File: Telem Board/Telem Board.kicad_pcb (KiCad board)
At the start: 2 copper layers, 27 parts, among them J1 MAIN, J2 NTC1, J3 NTC2, J4 NTC3, J5 NTC4, J6 6S, U1 LM1117-3.3, U2 MCP3208

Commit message: route
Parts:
- removed C9: 1uF, Capacitor_SMD:C_0805_2012Metric_Pad1.18x1.45mm_HandSolder
- removed H3, H4: MountingHole, MountingHole:MountingHole_3.2mm_M3
- H1, H2: footprint MountingHole:MountingHole_3.2mm_M3 -> MountingHole:MountingHole_2.7mm_M2.5
- moved J4 65.3 mm to (144.1, 99.7), turned to 270 degrees
- moved R5 62.9 mm to (149.2, 80.4), turned to 270 degrees
- moved J3 60.9 mm to (144.1, 94.0), turned to 270 degrees
- moved J5 57.4 mm to (144.1, 105.4), turned to 270 degrees
- moved C5 57.0 mm to (156.8, 80.9), turned to 90 degrees
- moved R6 56.8 mm to (153.0, 80.4), turned to 90 degrees
- moved J2 56.0 mm to (144.1, 88.3), turned to 270 degrees
- moved C2 55.1 mm to (153.7, 92.9), turned to 90 degrees
- moved C4 53.1 mm to (153.7, 104.4), turned to 90 degrees
- moved H1 52.1 mm to (141.6, 76.8)
- moved C3 50.1 mm to (153.7, 98.7), turned to 90 degrees
- moved C7 48.1 mm to (177.2, 73.7), turned to 270 degrees
- moved C6 47.3 mm to (168.3, 80.6)
- moved R3 47.1 mm to (149.9, 98.1), turned to 270 degrees
- moved J1 47.0 mm to (179.1, 85.7)
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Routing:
- net +3V3: track 0.00 -> 68.5 mm, vias 0 -> 6
- net /CH5: track 0.00 -> 19.0 mm
- net +5V: track 0.00 -> 18.2 mm
- net /CH4: track 0.00 -> 16.6 mm
- net /CH2: track 0.00 -> 16.6 mm
- net /CH3: track 0.00 -> 15.2 mm
- net /SPI_SCK: track 0.00 -> 14.4 mm
- net /SPI_MOSI: track 0.00 -> 14.4 mm
- net /SPI_MISO: track 0.00 -> 14.4 mm
- net /ADC_CS: track 0.00 -> 14.4 mm
- net /CH0: track 0.00 -> 13.5 mm
- net Net-(J6-Pad1): track 0.00 -> 8.57 mm
- net GNDA: track 0.00 -> 3.91 mm, vias 0 -> 4
- added copper zone on B.Cu, net GNDA
- added copper zone on F.Cu, net GNDA
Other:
- board outline added: 43.2 x 43.8 mm
- board text added: "100K NTC thermistors"
- board text added: "5V"
- board text added: "6S LIPO IN"
- board text added: "CS"
- board text added: "GND"
- board text added: "MISO"
- board text added: "MOSI"
- board text added: "SCK"
- board text added: "TJUAV Telemetry board v0.1 Alan Hsu"

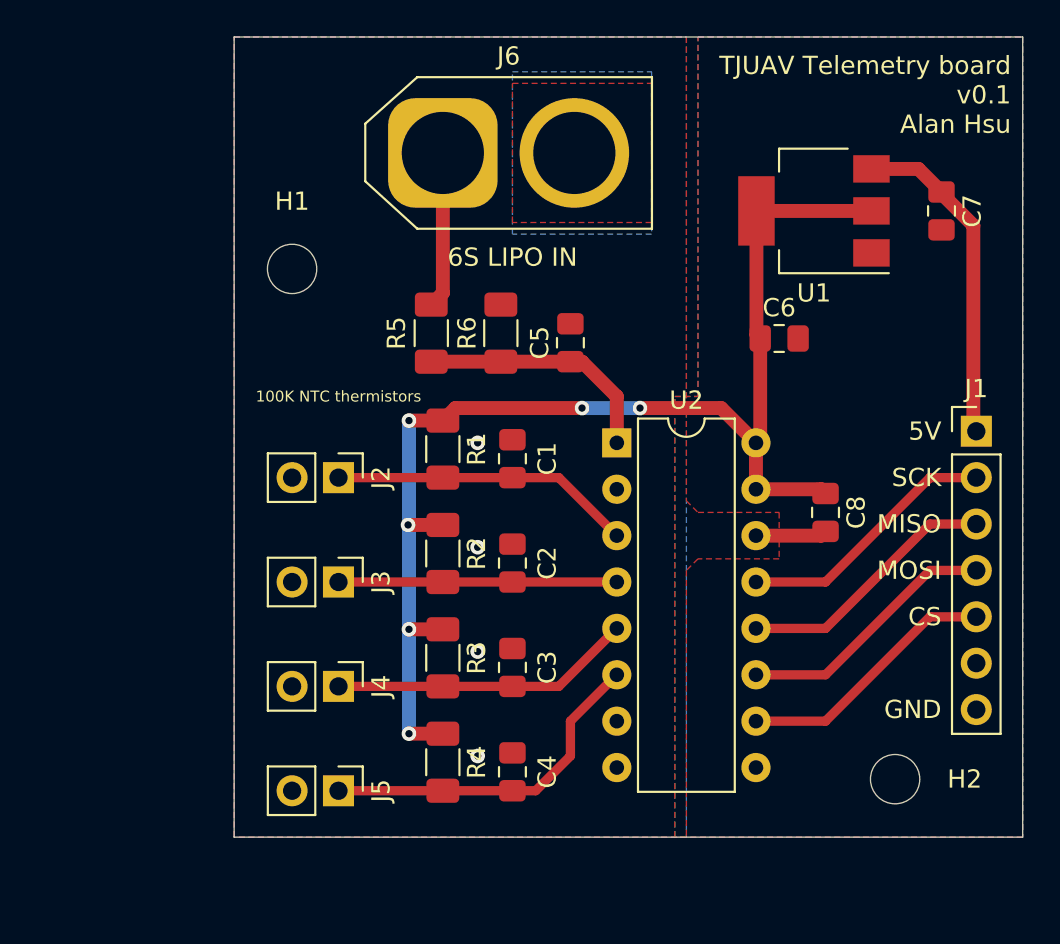
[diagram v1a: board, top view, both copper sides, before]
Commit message: add 3s battery in
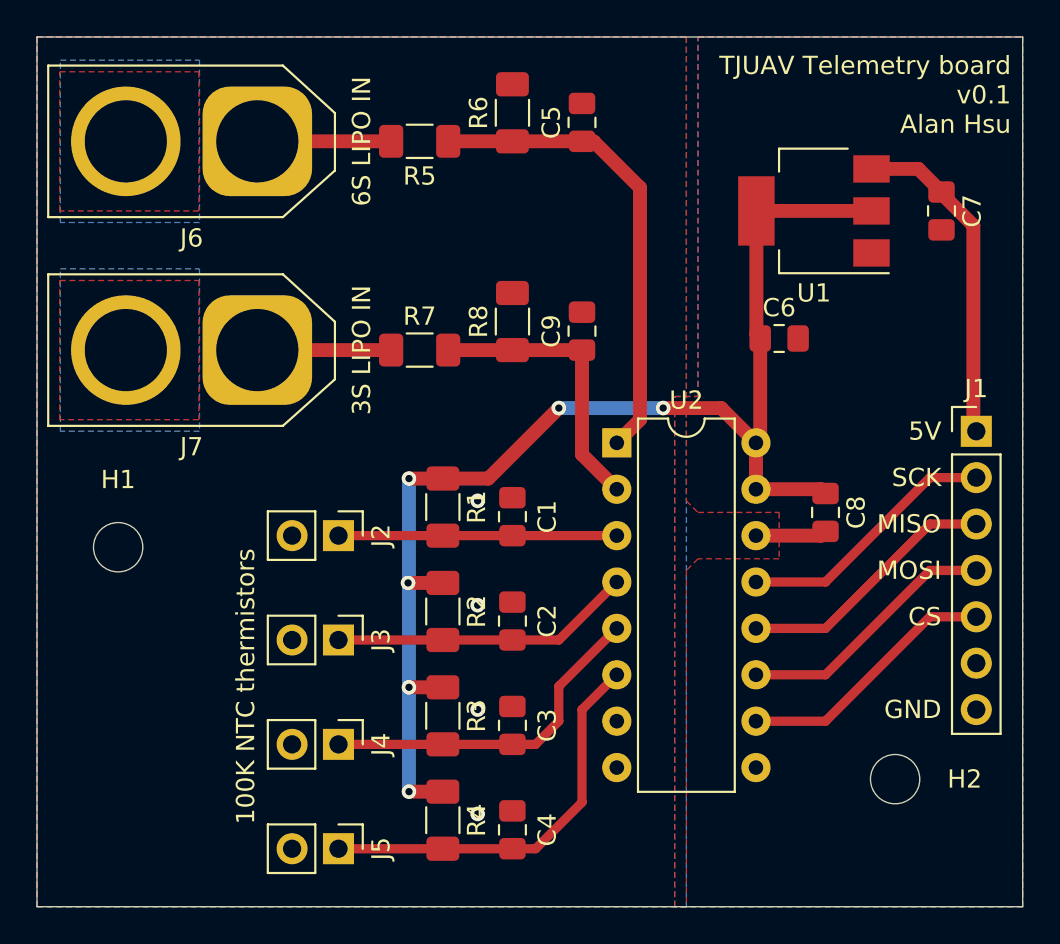
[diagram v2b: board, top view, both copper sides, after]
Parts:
- added C9: 0.47uF, Capacitor_SMD:C_0805_2012Metric_Pad1.18x1.45mm_HandSolder, F.Cu at (157.5, 80.2)
- added J7: 3S, Connector_AMASS:AMASS_XT60-M_1x02_P7.20mm_Vertical, F.Cu at (139.7, 81.3)
- added R7: 200K, Capacitor_SMD:C_1206_3216Metric_Pad1.33x1.80mm_HandSolder, F.Cu at (148.6, 81.3)
- added R8: 42K, Capacitor_SMD:C_1206_3216Metric_Pad1.33x1.80mm_HandSolder, F.Cu at (153.7, 79.7)
- moved H1 18.0 mm to (132.1, 92.1)
- moved R6 12.1 mm to (153.7, 68.3)
- moved C5 12.1 mm to (157.5, 68.8)
- moved R5 10.5 mm to (148.6, 69.8), turned to 0 degrees
- moved J6 10.2 mm to (139.7, 69.8), turned to 180 degrees
- moved C2 3.18 mm to (153.7, 96.1)
- moved J4 3.18 mm to (144.1, 102.9)
- moved R3 3.18 mm to (149.9, 101.3)
- moved C1 3.17 mm to (153.7, 90.4)
- moved C3 3.17 mm to (153.7, 101.8)
- moved C4 3.17 mm to (153.7, 107.5)
- moved J2 3.17 mm to (144.1, 91.4)
- moved J3 3.17 mm to (144.1, 97.2)
- moved J5 3.17 mm to (144.1, 108.6)
- moved R1 3.17 mm to (149.9, 89.9)
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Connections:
- U2 pad 2: (no net) -> /CH1
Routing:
- net /CH1: track 0.00 -> 15.7 mm
- net /CH0: track 13.5 -> 26.1 mm
- net Net-(J7-Pad1): track 0.00 -> 7.33 mm
- net /CH5: track 19.0 -> 22.2 mm
- net /CH4: track 16.6 -> 19.0 mm
- net /CH3: track 15.2 -> 16.6 mm
- net /CH2: track 16.6 -> 15.2 mm
- net +3V3: track 68.5 -> 69.8 mm
- net Net-(J6-Pad1): track 8.57 -> 7.33 mm
- added copper zone on B.Cu, net (none)
- added copper zone on F.Cu, net (none)
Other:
- board size 43.2 x 43.8 mm -> 54 x 47.6 mm
- board text added: "3S LIPO IN"

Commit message: gerbers
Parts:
- added F1: 125mA, Resistor_SMD:R_1206_3216Metric_Pad1.30x1.75mm_HandSolder, F.Cu at (147.3, 68.3)
- added F2: 125mA, Resistor_SMD:R_1206_3216Metric_Pad1.30x1.75mm_HandSolder, F.Cu at (147.3, 79.7)
- moved R5 2.46 mm to (150.5, 68.3), turned to 270 degrees
- moved R7 2.46 mm to (150.5, 79.7), turned to 270 degrees
- moved R6 0.64 mm to (154.3, 68.3)
- moved R8 0.64 mm to (154.3, 79.7)
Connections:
- J6 pad 1: Net-(J6-Pad1) -> Net-(F1-Pad2)
- J7 pad 1: Net-(J7-Pad1) -> Net-(F2-Pad2)
- R5 pad 1: Net-(J6-Pad1) -> Net-(F1-Pad1)
- R7 pad 1: Net-(J7-Pad1) -> Net-(F2-Pad1)
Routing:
- net Net-(F2-Pad2): track 0.00 -> 7.62 mm
- net Net-(F1-Pad2): track 0.00 -> 7.62 mm
- net Net-(J7-Pad1): track 7.33 -> 0.00 mm
- net Net-(J6-Pad1): track 7.33 -> 0.00 mm
- net Net-(F2-Pad1): track 0.00 -> 3.19 mm
- net Net-(F1-Pad1): track 0.00 -> 3.19 mm
- removed copper zone on B.Cu, net (none)
- removed copper zone on F.Cu, net (none)

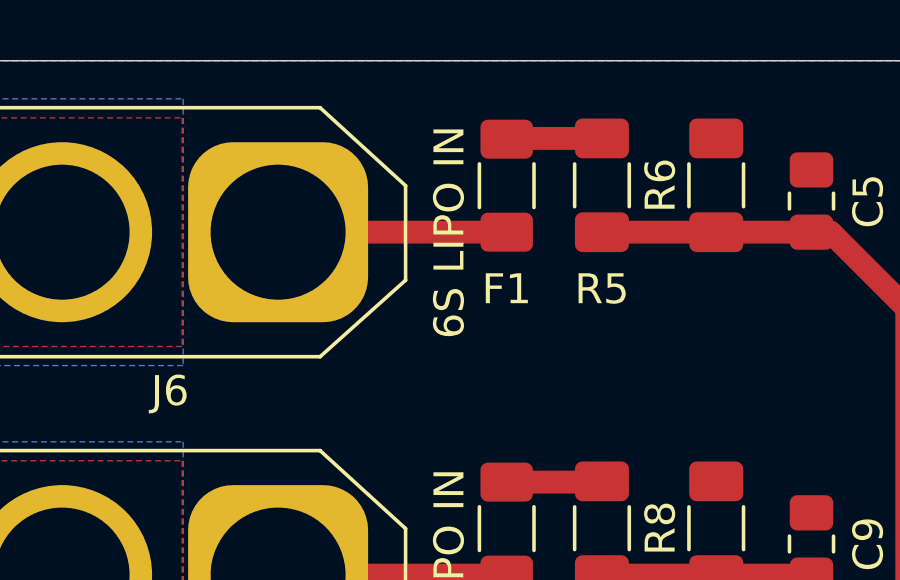
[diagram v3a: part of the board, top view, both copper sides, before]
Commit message: use 12s resistor sizes instead of 6s
#1
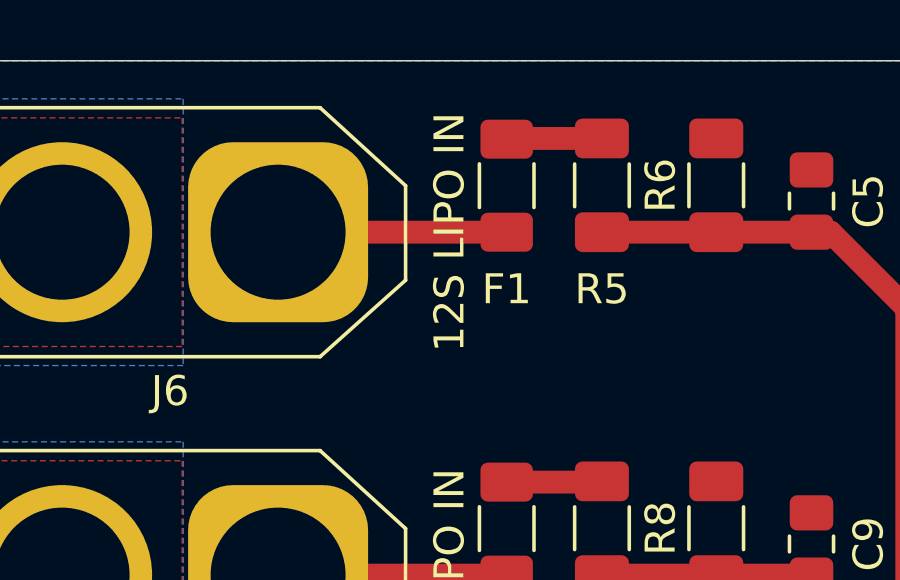
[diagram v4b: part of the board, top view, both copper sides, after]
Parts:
- J6: value 6S -> 12S
- R5: value 250K -> 470K
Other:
- board text added: "12S LIPO IN"
- board text removed: "6S LIPO IN"

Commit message: update gerbers
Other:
- board text added: "TJUAV Telemetry board v1.0 Alan Hsu"
- board text removed: "TJUAV Telemetry board v0.1 Alan Hsu"

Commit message: update values
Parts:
- R6: value 27K -> 22K
- R8: value 42K -> 43K
